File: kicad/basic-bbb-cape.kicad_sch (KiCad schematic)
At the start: 2 parts

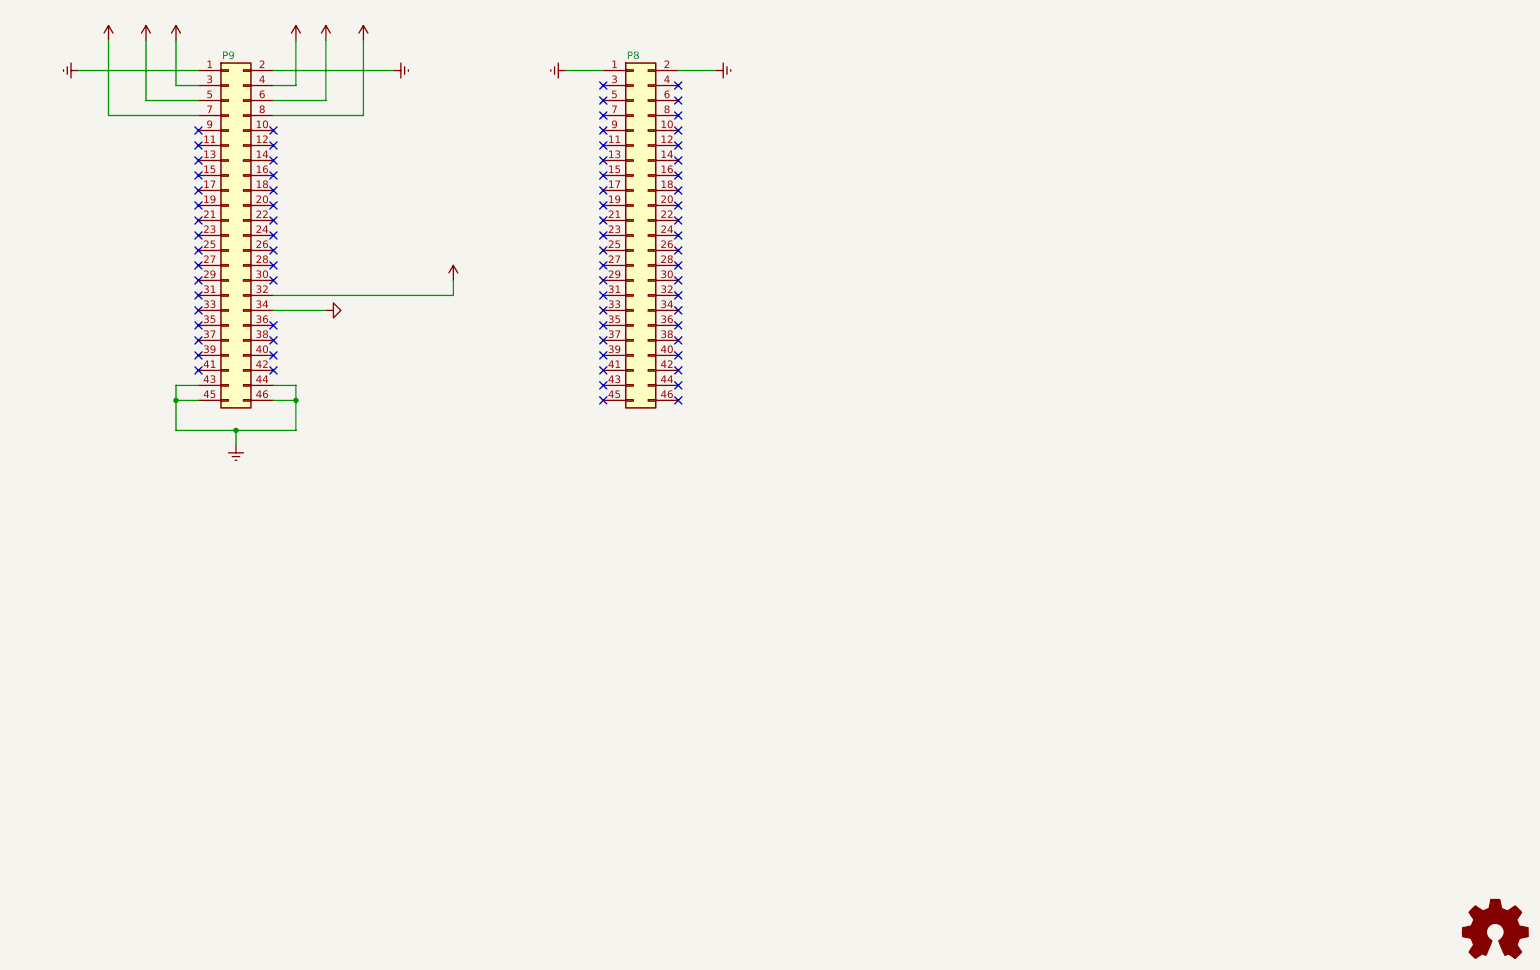
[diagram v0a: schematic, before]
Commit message: kicad: Multiple changes including adding
sym-lib-table,
Beaglebone_black_p8.kicad_sym, and
Beaglebone_black_p9.kicad_sym.
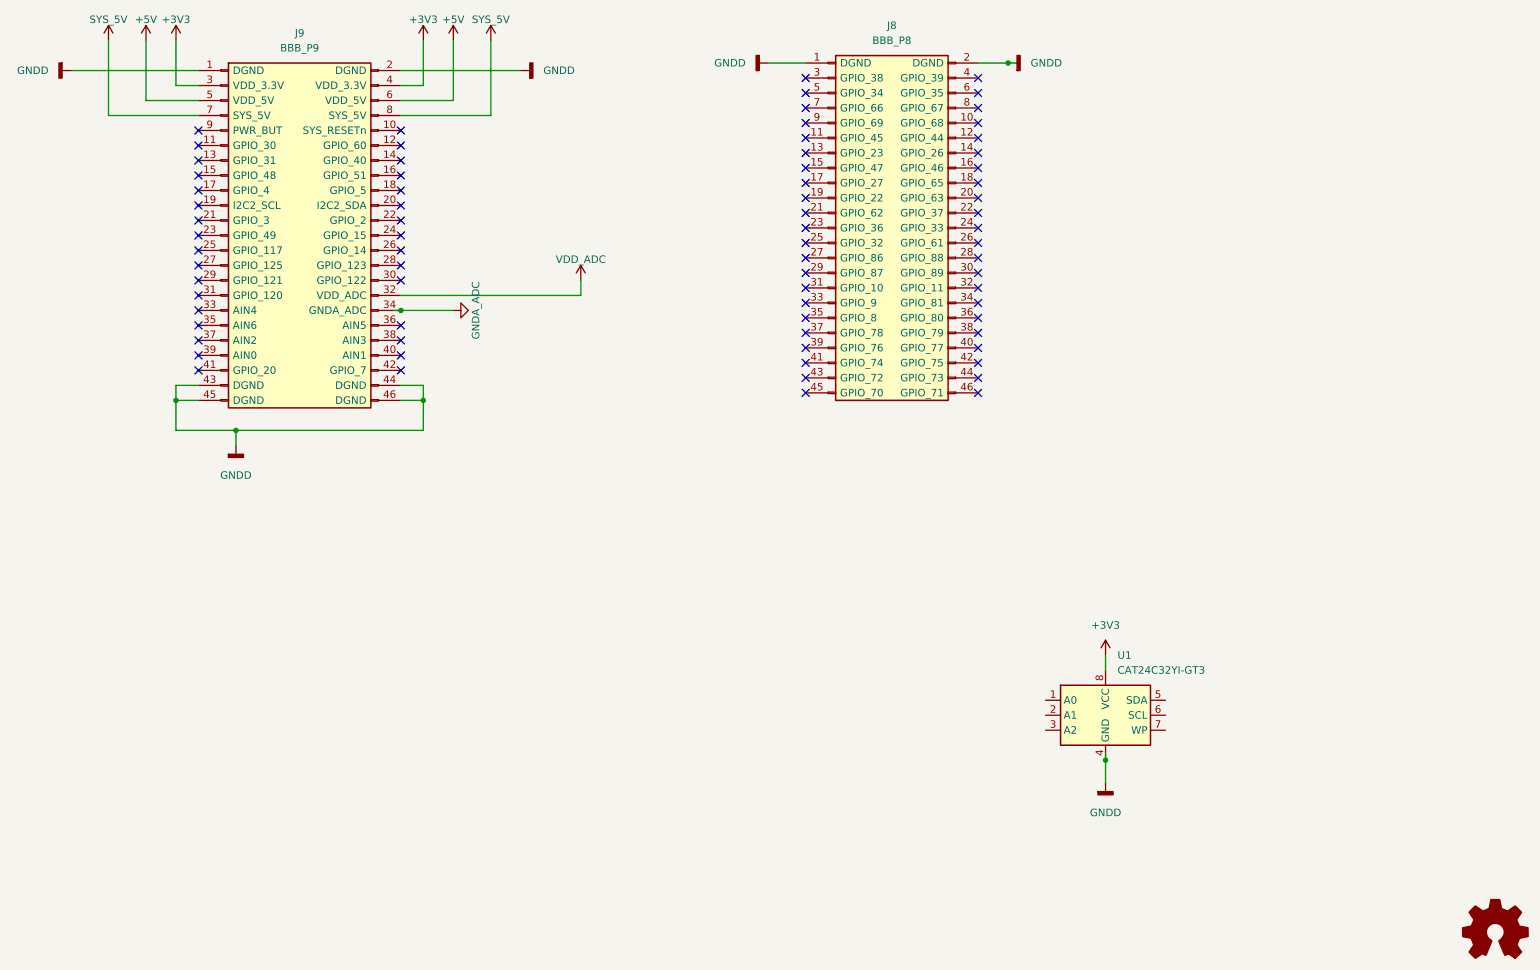
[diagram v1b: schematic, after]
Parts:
- removed P8, P9: (no value), symbol Connector_Generic:Conn_02x23_Odd_Even
- added J8: BBB_P8, Socket_BeagleBone_Black:Socket_BeagleBone_Black, symbol Beaglebone_black_p8:BBB_P8
- added J9: BBB_P9, Socket_BeagleBone_Black:Socket_BeagleBone_Black, symbol Beaglebone_black_p9:BBB_P9
- added U1: CAT24C32YI-GT3, Package_SO:HTSOP-8-1EP_3.9x4.9mm_P1.27mm_EP2.4x3.2mm, symbol Memory_EEPROM:24LC32
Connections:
- net +3V3: now also J9.3 (VDD_3.3V), J9.4 (VDD_3.3V), U1.8 (VCC)
- net +5V: now also J9.5 (VDD_5V), J9.6 (VDD_5V)
- net GNDA_ADC: now also J9.34 (GNDA_ADC)
- net SYS_5V: now also J9.7 (SYS_5V), J9.8 (SYS_5V)
- net VDD_ADC: now also J9.32 (VDD_ADC)
- new net GNDD: J8.1 (DGND), J8.2 (DGND), J9.1 (DGND), J9.2 (DGND), J9.43 (DGND), J9.44 (DGND), J9.45 (DGND), J9.46 (DGND), U1.4 (GND)
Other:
- title: Doorlockd - BBB PCB -> (none)
